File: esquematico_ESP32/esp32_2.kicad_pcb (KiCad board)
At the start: 2 copper layers, 95.2 x 97.9 mm, 42 parts, among them J1 Conn_01x05_Female, J2 Conn_01x08_Female, J3 Conn_01x08_Female, J4 USB_A, J5 Conn_01x14_Female, J6 Conn_01x04_Female, J7 Jack-DC, Q1 BSS138, Q2 BSS138, SW1 SW_Push, SW2 SW_Push, U1 ESP32-WROOM-32, U2 LM1117-3.3, U3 LM2596S-5

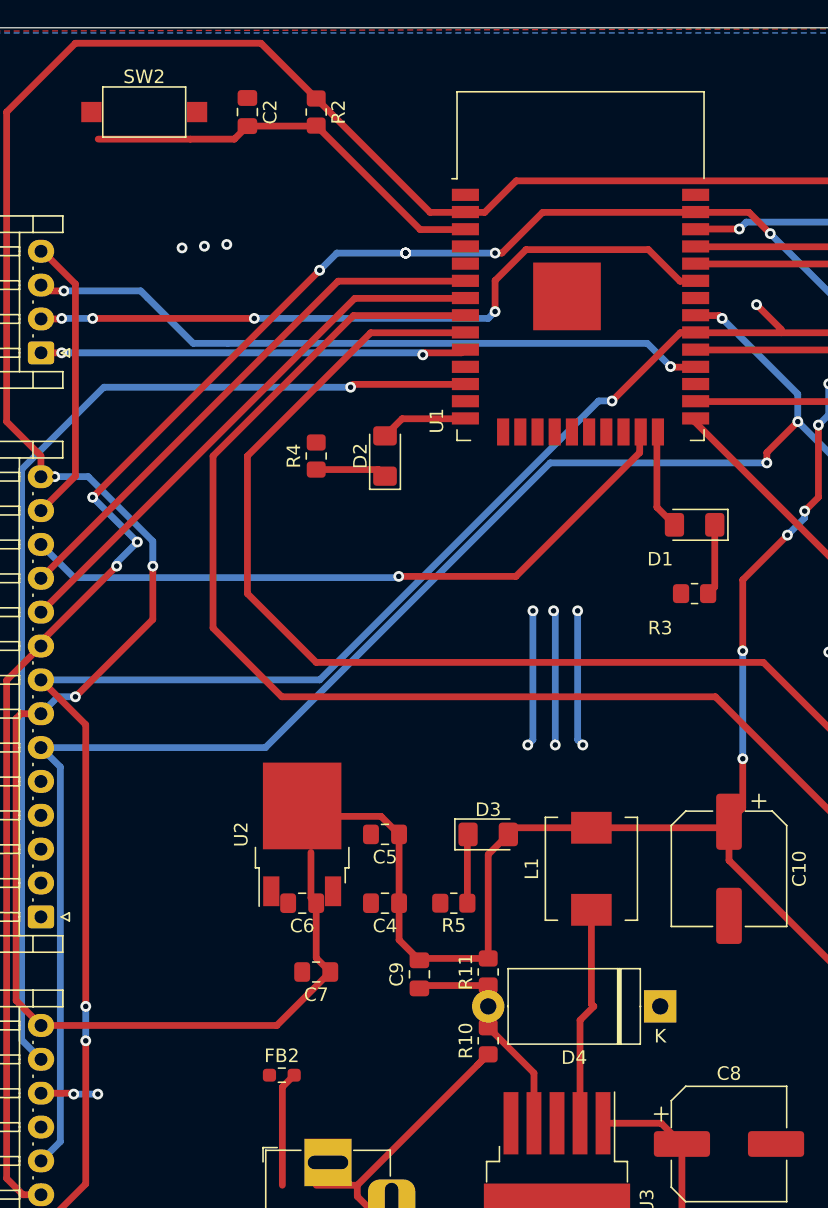
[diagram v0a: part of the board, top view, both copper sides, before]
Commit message: listo para rutear la ESP
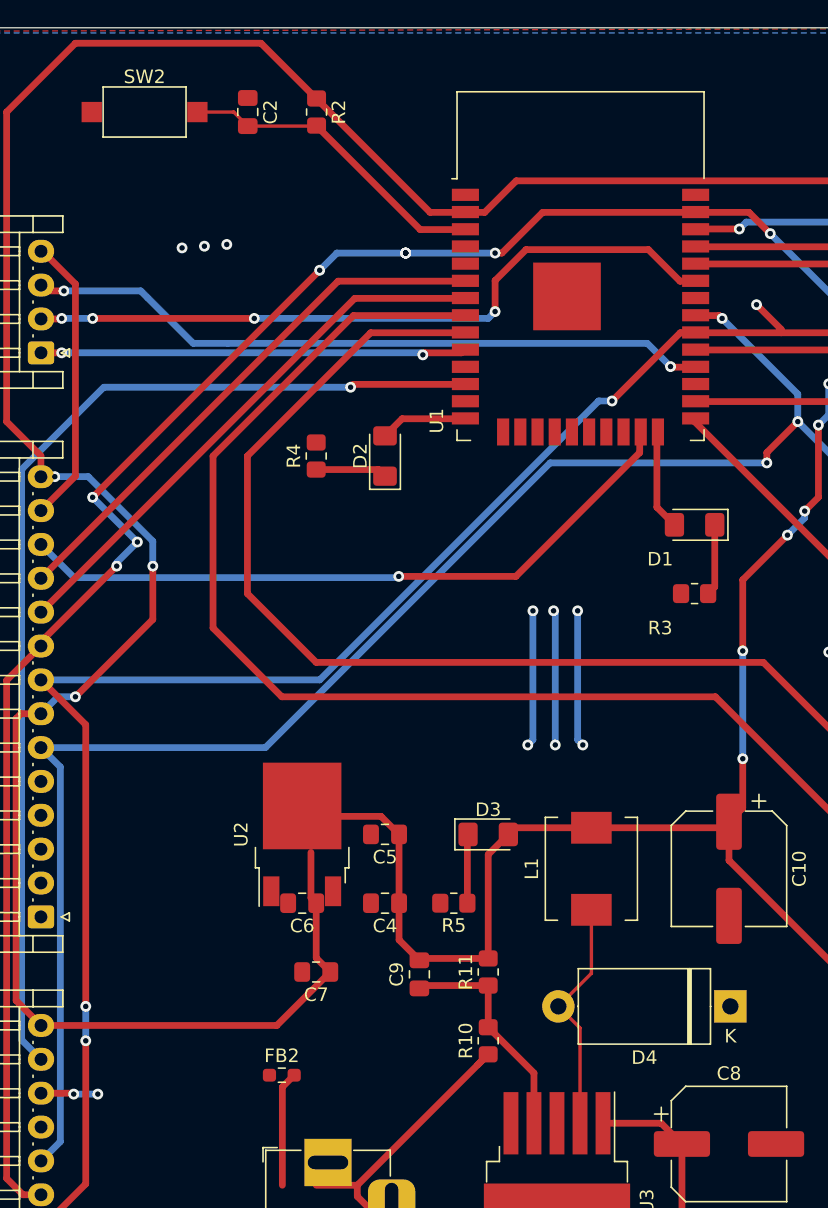
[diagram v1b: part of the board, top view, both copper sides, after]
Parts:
- moved D4 5.18 mm to (152.5, 101.6)
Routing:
- net /EN: track 30.6 -> 23.4 mm
- net Net-(D4-Pad2): track 16.3 -> 17.4 mm
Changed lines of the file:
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@@
   )
   (footprint "Button_Switch_SMD:SW_SPST_CK_RS282G05A3" (layer "F.Cu")
-    (at 109.22 35.56)
+    (at 109.2454 35.56)
     (descr "https://www.mouser.com/ds/2/60/RS-282G05A-SM_RT-1159762.pdf")
     (tags "SPST button tactile switch")
@@
   )
   (footprint "Resistor_SMD:R_0805_2012Metric_Pad1.20x1.40mm_HandSolder" (layer "F.Cu")
-    (at 121.92 35.56 -90)
+    (at 121.9454 35.56 -90)
     (descr "Resistor SMD 0805 (2012 Metric), square (rectangular) end terminal, IPC_7351 nominal with elongated pad for handsoldering. (Body size source: IPC-SM-782 page 72, https://www.pcb-3d.com/wordpress/wp-content/uploads/ipc-sm-782a_amendment_1_and_2.pdf), generated with kicad-footprint-generator")
     (tags "resistor handsolder")
@@
   )
   (footprint "Diode_THT:D_DO-27_P12.70mm_Horizontal" (layer "F.Cu")
-    (at 147.32 101.6 180)
+    (at 152.5016 101.6 180)
     (descr "Diode, DO-27 series, Axial, Horizontal, pin pitch=12.7mm, , length*diameter=9.52*5.33mm^2, , http://www.slottechforum.com/slotinfo/Techstuff/CD2%20Diodes%20and%20Transistors/Cases/Diode%20DO-27.jpg")
     (tags "Diode DO-27 series Axial Horizontal pin pitch 12.7mm  length 9.52mm diameter 5.33mm")
@@
   )
   (footprint "Capacitor_SMD:C_0805_2012Metric_Pad1.18x1.45mm_HandSolder" (layer "F.Cu")
-    (at 116.84 35.56 -90)
+    (at 116.8654 35.56 -90)
     (descr "Capacitor SMD 0805 (2012 Metric), square (rectangular) end terminal, IPC_7351 nominal with elongated pad for handsoldering. (Body size source: IPC-SM-782 page 76, https://www.pcb-3d.com/wordpress/wp-content/uploads/ipc-sm-782a_amendment_1_and_2.pdf, https://docs.google.com/spreadsheets/d/1BsfQQcO9C6DZCsRaXUlFlo91Tg2WpOkGARC1WS5S8t0/edit?usp=sharing), generated with kicad-footprint-generator")
     (tags "capacitor handsolder")
@@
   (segment (start 153.416 75.3505) (end 153.416 83.312) (width 0.5) (layer "B.Cu") (net 2))
   (segment (start 171.45 91.186) (end 171.958 90.678) (width 0.5) (layer "B.Cu") (net 2))
+  (segment (start 121.9454 36.56) (end 121.9079 36.5975) (width 0.25) (layer "F.Cu") (net 3))
   (segment (start 121.8825 36.5975) (end 121.92 36.56) (width 0.5) (layer "F.Cu") (net 3))
-  (segment (start 105.82 37.56) (end 112.62 37.56) (width 0.5) (layer "F.Cu") (net 3))
-  (segment (start 115.8775 37.56) (end 116.84 36.5975) (width 0.5) (layer "F.Cu") (net 3))
   (segment (start 121.92 36.56) (end 129.599 44.239) (width 0.5) (layer "F.Cu") (net 3))
-  (segment (start 112.62 37.56) (end 115.8775 37.56) (width 0.5) (layer "F.Cu") (net 3))
   (segment (start 129.599 44.239) (end 132.86 44.239) (width 0.5) (layer "F.Cu") (net 3))
-  (segment (start 116.84 36.5975) (end 121.8825 36.5975) (width 0.5) (layer "F.Cu") (net 3))
+  (segment (start 115.8279 35.56) (end 113.1454 35.56) (width 0.25) (layer "F.Cu") (net 3))
+  (segment (start 116.8654 36.5975) (end 115.8279 35.56) (width 0.25) (layer "F.Cu") (net 3))
+  (segment (start 121.9079 36.5975) (end 116.8654 36.5975) (width 0.25) (layer "F.Cu") (net 3))
   (segment (start 134.62 105.14) (end 133.850489 105.909511) (width 0.5) (layer "F.Cu") (net 5))
   (segment (start 148.925 121.154022) (end 145.549511 124.529511) (width 0.5) (layer "F.Cu") (net 5))
@@
   (segment (start 134.62 103.14) (end 134.62 100.06) (width 0.5) (layer "F.Cu") (net 12))
   (segment (start 138 106.52) (end 134.62 103.14) (width 0.5) (layer "F.Cu") (net 12))
-  (segment (start 141.4 102.62) (end 141.4 110.23) (width 0.5) (layer "F.Cu") (net 13))
-  (segment (start 142.24 101.42) (end 142.42 101.6) (width 0.5) (layer "F.Cu") (net 13))
-  (segment (start 142.42 101.6) (end 141.4 102.62) (width 0.5) (layer "F.Cu") (net 13))
-  (segment (start 142.24 94.47) (end 142.24 101.42) (width 0.5) (layer "F.Cu") (net 13))
+  (segment (start 142.24 99.1616) (end 139.8016 101.6) (width 0.25) (layer "F.Cu") (net 13))
+  (segment (start 139.8016 101.6) (end 141.4 103.1984) (width 0.25) (layer "F.Cu") (net 13))
+  (segment (start 142.24 94.47) (end 142.24 99.1616) (width 0.25) (layer "F.Cu") (net 13))
+  (segment (start 141.4 103.1984) (end 141.4 110.23) (width 0.25) (layer "F.Cu") (net 13))
   (segment (start 123.5335 48.049) (end 132.86 48.049) (width 0.5) (layer "F.Cu") (net 14))
   (segment (start 101.5925 69.99) (end 123.5335 48.049) (width 0.5) (layer "F.Cu") (net 14))

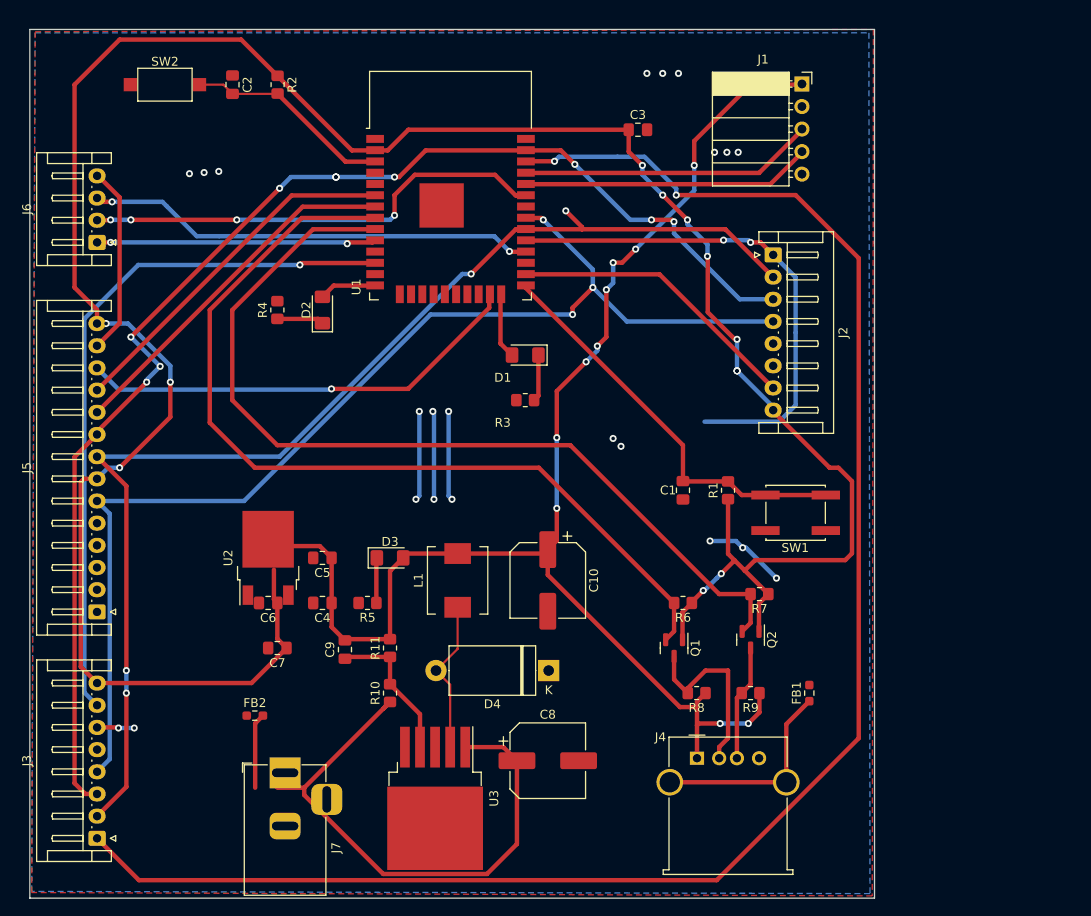
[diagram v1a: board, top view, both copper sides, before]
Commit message: ruteo listo con un posible error en footprint esp32
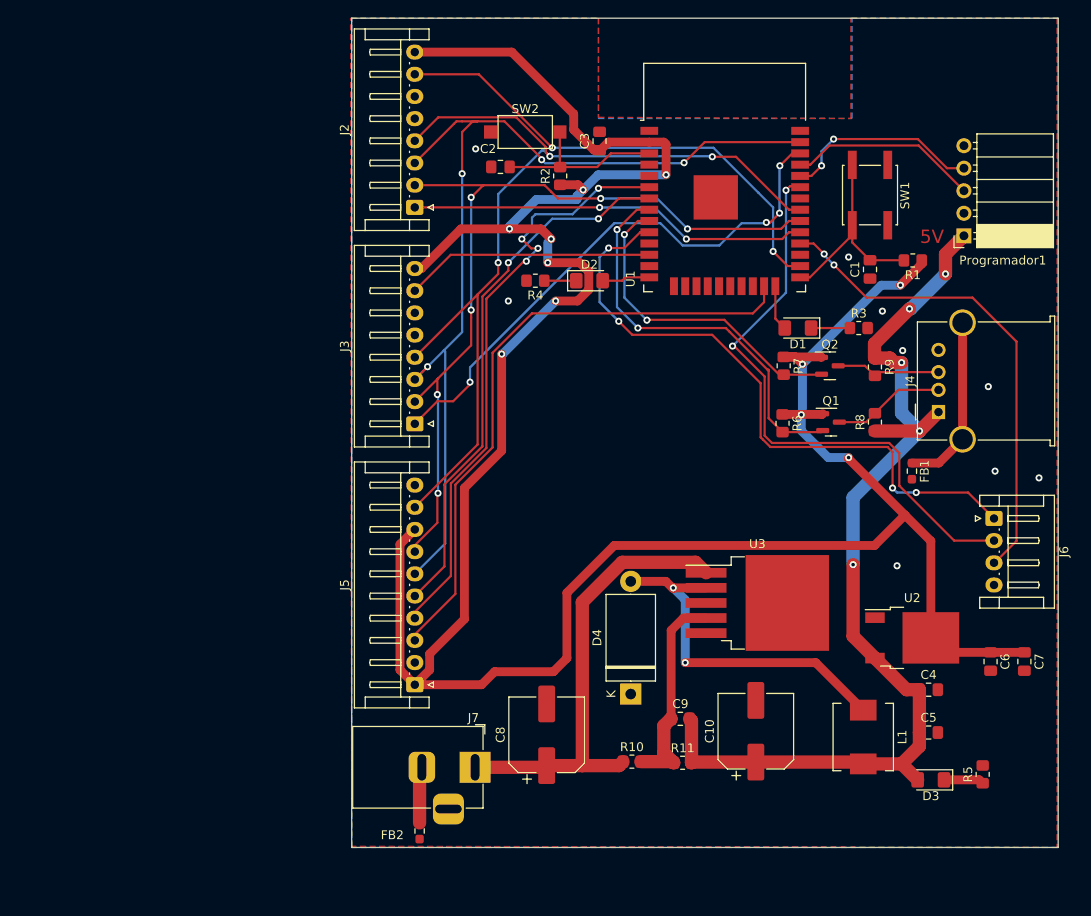
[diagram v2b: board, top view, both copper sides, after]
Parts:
- removed J1: Conn_01x05_Female, Connector_PinSocket_2.54mm:PinSocket_1x05_P2.54mm_Horizontal
- added Programador1: Conn_01x05_Female, Connector_PinSocket_2.54mm:PinSocket_1x05_P2.54mm_Horizontal, F.Cu at (199.3, 52.6)
- J2: value Conn_01x08_Female -> Conn_RFID1
- J3: value Conn_01x08_Female -> Conn_RFID2
- J5: value Conn_01x14_Female -> Conn_screen; footprint Connector_JST:JST_EH_S14B-EH_1x14_P2.50mm_Horizontal -> Connector_JST:JST_EH_S10B-EH_1x10_P2.50mm_Horizontal
- SW2: value SW_Push -> Enable
- moved J6 105.8 mm to (202.7, 84.5), turned to -90 degrees
- moved C7 84.2 mm to (206.1, 100.6), turned to -90 degrees
- moved C6 81.7 mm to (202.3, 100.6), turned to -90 degrees
- moved U2 73.2 mm to (193.5, 97.9), turned to 0 degrees
- moved R5 72.0 mm to (201.4, 113.3), turned to 90 degrees
- moved C5 71.1 mm to (195.3, 108.6), turned to 0 degrees
- moved C4 69.0 mm to (195.3, 103.8), turned to 0 degrees
- moved D3 65.9 mm to (195.6, 113.9), turned to 180 degrees
- moved J3 58.9 mm to (137.4, 73.8)
- moved L1 49.0 mm to (188.0, 109.1), turned to -90 degrees
- moved J4 47.6 mm to (196.4, 72.5), turned to 90 degrees
- moved U3 42.5 mm to (176.0, 94.0), turned to 0 degrees
- moved SW2 41.0 mm to (149.9, 40.9)
- moved J2 40.8 mm to (137.4, 49.4), turned to 90 degrees
- moved R9 39.3 mm to (189.3, 67.4), turned to -90 degrees
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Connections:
- C4 pad 2: Net-(C4-Pad2) -> GND
- C5 pad 2: Net-(C4-Pad2) -> GND
- C6 pad 2: Net-(C4-Pad2) -> GND
- C7 pad 2: Net-(C4-Pad2) -> GND
- J5 pad 1: unconnected-(J5-Pad1) -> +3V3
- J5 pad 10: /D/C -> unconnected-(J5-Pad10)
- J5 pad 2: unconnected-(J5-Pad2) -> GND
- J5 pad 3: unconnected-(J5-Pad3) -> /CS_Display
- J5 pad 4: unconnected-(J5-Pad4) -> /RST_D
- J5 pad 5: unconnected-(J5-Pad5) -> /D/C
- J5 pad 6: /MISO -> /MOSI
- J5 pad 7: +3V3 -> /SCK
- J5 pad 8: /SCK -> +3V3
- J5 pad 9: /MOSI -> /MISO
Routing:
- net +3V3: track 445.0 -> 308.2 mm, vias 22 -> 11
- net /CS_LECTOR_2: track 191.5 -> 62.3 mm, vias 2 -> 4
- net +5V: track 0.00 -> 114.7 mm, vias 0 -> 5
- net /DATA_KEYBOARD: track 102.0 -> 36.4 mm, vias 0 -> 2
- net GND: track 64.9 -> 0.00 mm, vias 22 -> 9
- net /CLC_KEYBOARD: track 100.8 -> 45.6 mm, vias 0 -> 2
- net /RST_2: track 79.4 -> 28.1 mm, vias 1 -> 0
- net /MAGNE_3: track 31.5 -> 72.3 mm, vias 2 -> 4
- net /SCK: track 135.2 -> 94.3 mm, vias 4 -> 6
- net /MOSI: track 147.5 -> 109.4 mm, vias 11 -> 4
- net /RST_D: track 40.4 -> 67.4 mm, vias 0 -> 4
- net /MISO: track 132.0 -> 106.6 mm
- net Net-(D4-Pad2): track 17.4 -> 40.1 mm, vias 0 -> 2
- net /RST_1: track 33.3 -> 55.3 mm, vias 0 -> 2
- net /IOD: track 46.2 -> 24.4 mm
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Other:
- board size 95.2 x 97.9 mm -> 79.6 x 93.5 mm
- board text added: "5V"
